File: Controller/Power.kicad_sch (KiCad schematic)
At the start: 27 parts, among them Q31 RJK0654DPB-00-J5, SW31 PTS815 SJM 250 SMTR LFS, U31 AP63203WU, U32 SN74LVC1G08DBVR

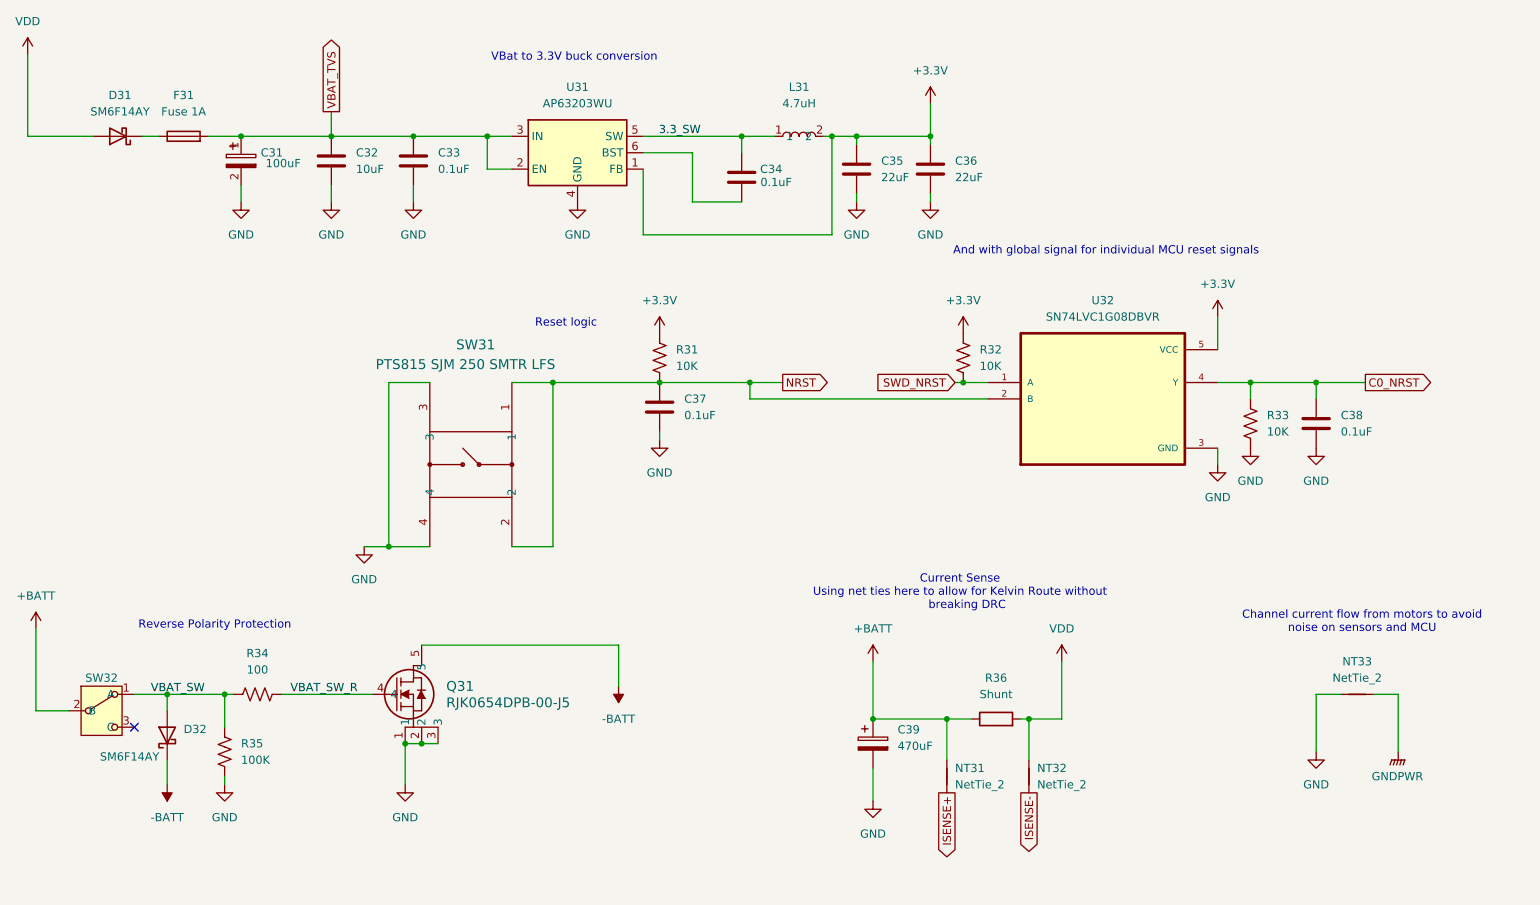
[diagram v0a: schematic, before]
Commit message: Finished Schematic for controller
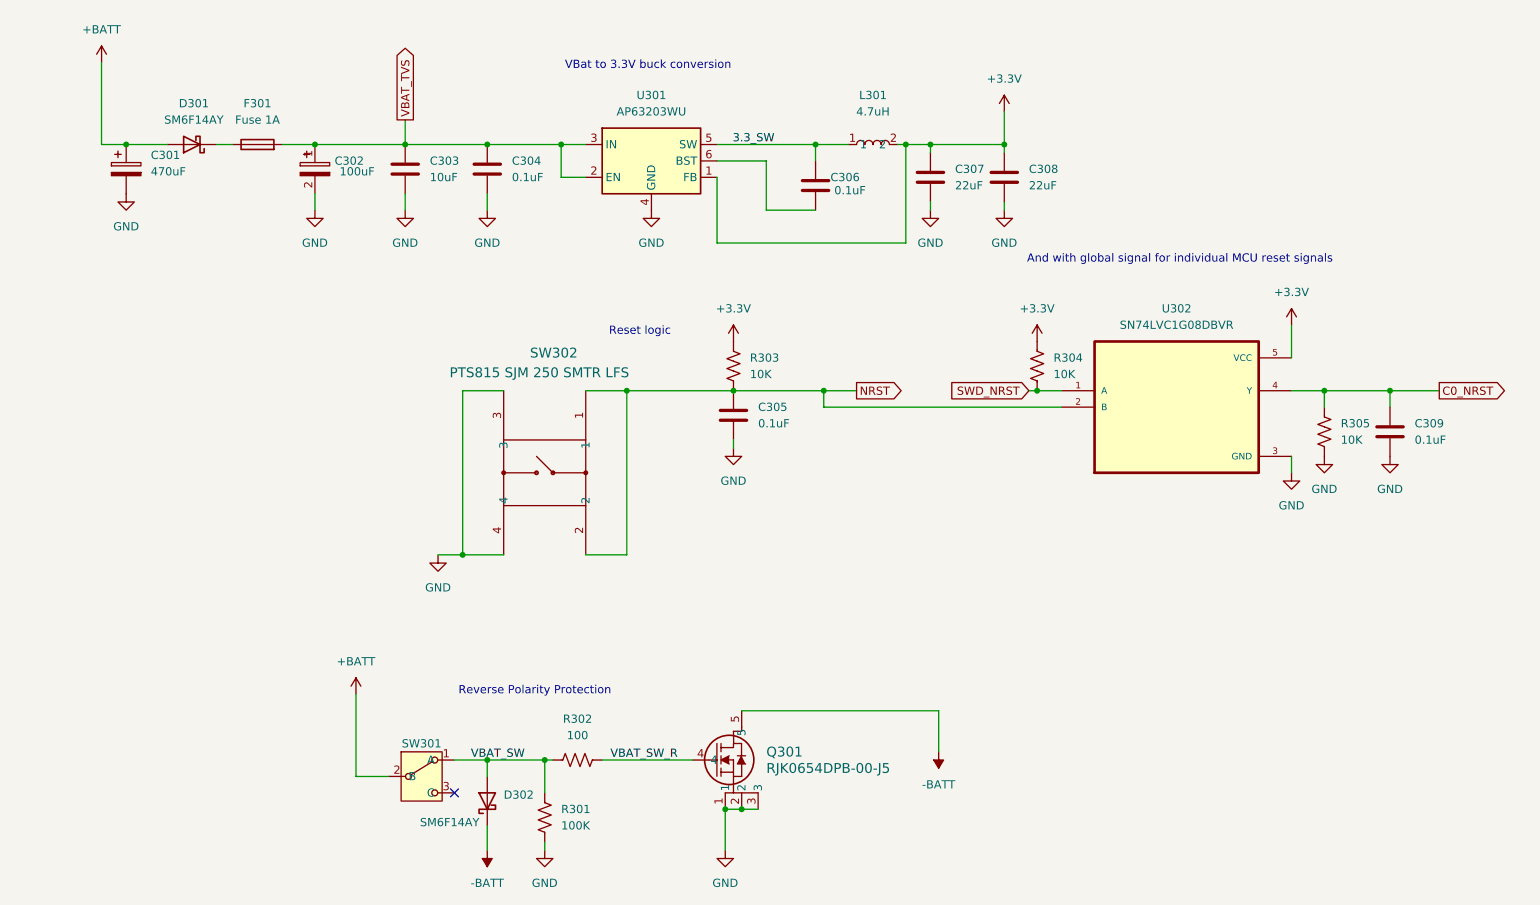
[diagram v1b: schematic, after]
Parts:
- removed C39: 470uF, Capacitor_SMD:CP_Elec_10x10.5, symbol Device:C_Polarized
- removed NT31, NT32: NetTie_2, NetTie:NetTie-2_SMD_Pad0.5mm, symbol Device:NetTie_2
- removed NT33: NetTie_2, NetTie:NetTie-2_SMD_Pad2.0mm, symbol Device:NetTie_2
- removed R36: Shunt, Resistor_SMD:R_2010_5025Metric, symbol Device:R
- added C301: 470uF, Capacitor_SMD:CP_Elec_10x10.5, symbol Device:C_Polarized
- renumbered C31 to C302, C32 to C303, C33 to C304, C37 to C305, C34 to C306, C35 to C307, C36 to C308, C38 to C309, D31 to D301, D32 to D302, F31 to F301, L31 to L301, Q31 to Q301, R35 to R301, R34 to R302, R31 to R303, R32 to R304, R33 to R305, SW32 to SW301, SW31 to SW302, U31 to U301, U32 to U302
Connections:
- net VDD is gone; now on net +BATT: D301.2 (A)
- net +BATT: now also C301.1
- net GND: now also C301.2
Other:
- note removed: "Channel current flow from motors to avoid noise on sensors and MCU"
- note removed: "Current Sense Using net ties here to allow for Kelvin Route without breaking DRC"
- moved on the sheet: C302, C303, C304, C305, C306, C307, C308, C309, D301, D302, F301, L301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
